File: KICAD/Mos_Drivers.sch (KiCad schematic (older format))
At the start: 15 parts, among them U12 UCC27284-Q1

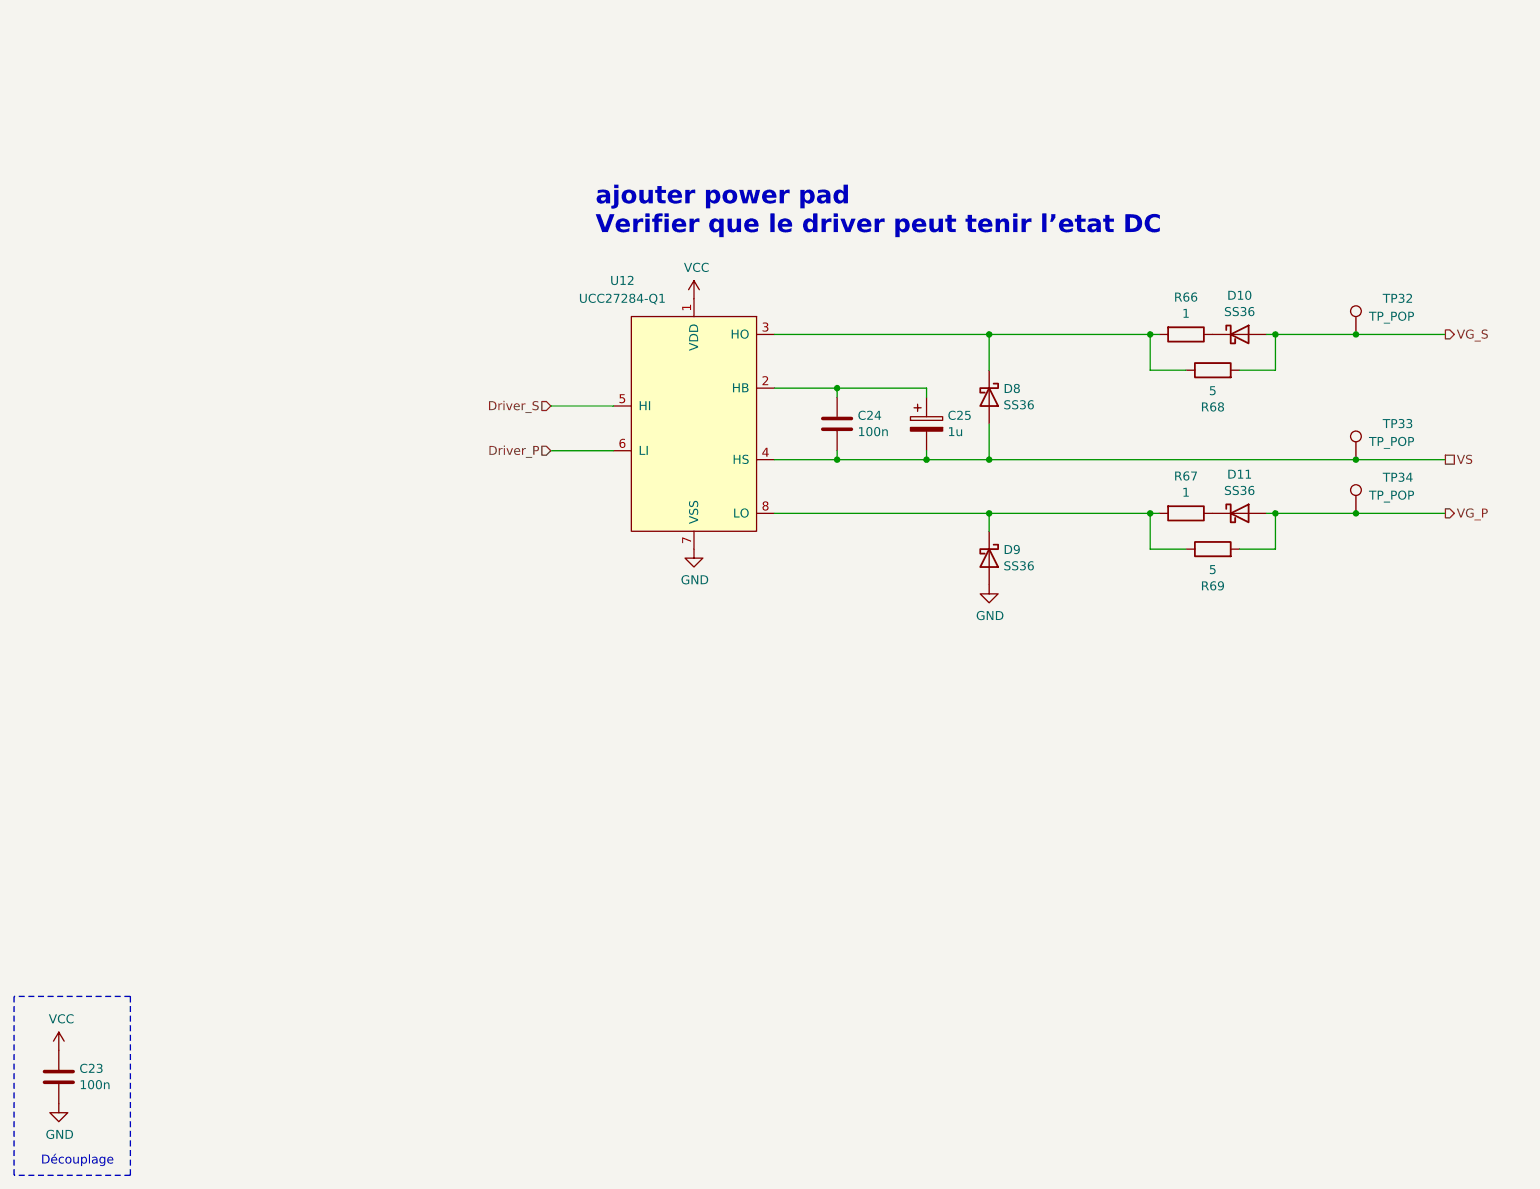
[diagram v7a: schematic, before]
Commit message: added footprint for sepic coil + no more errors in netlist
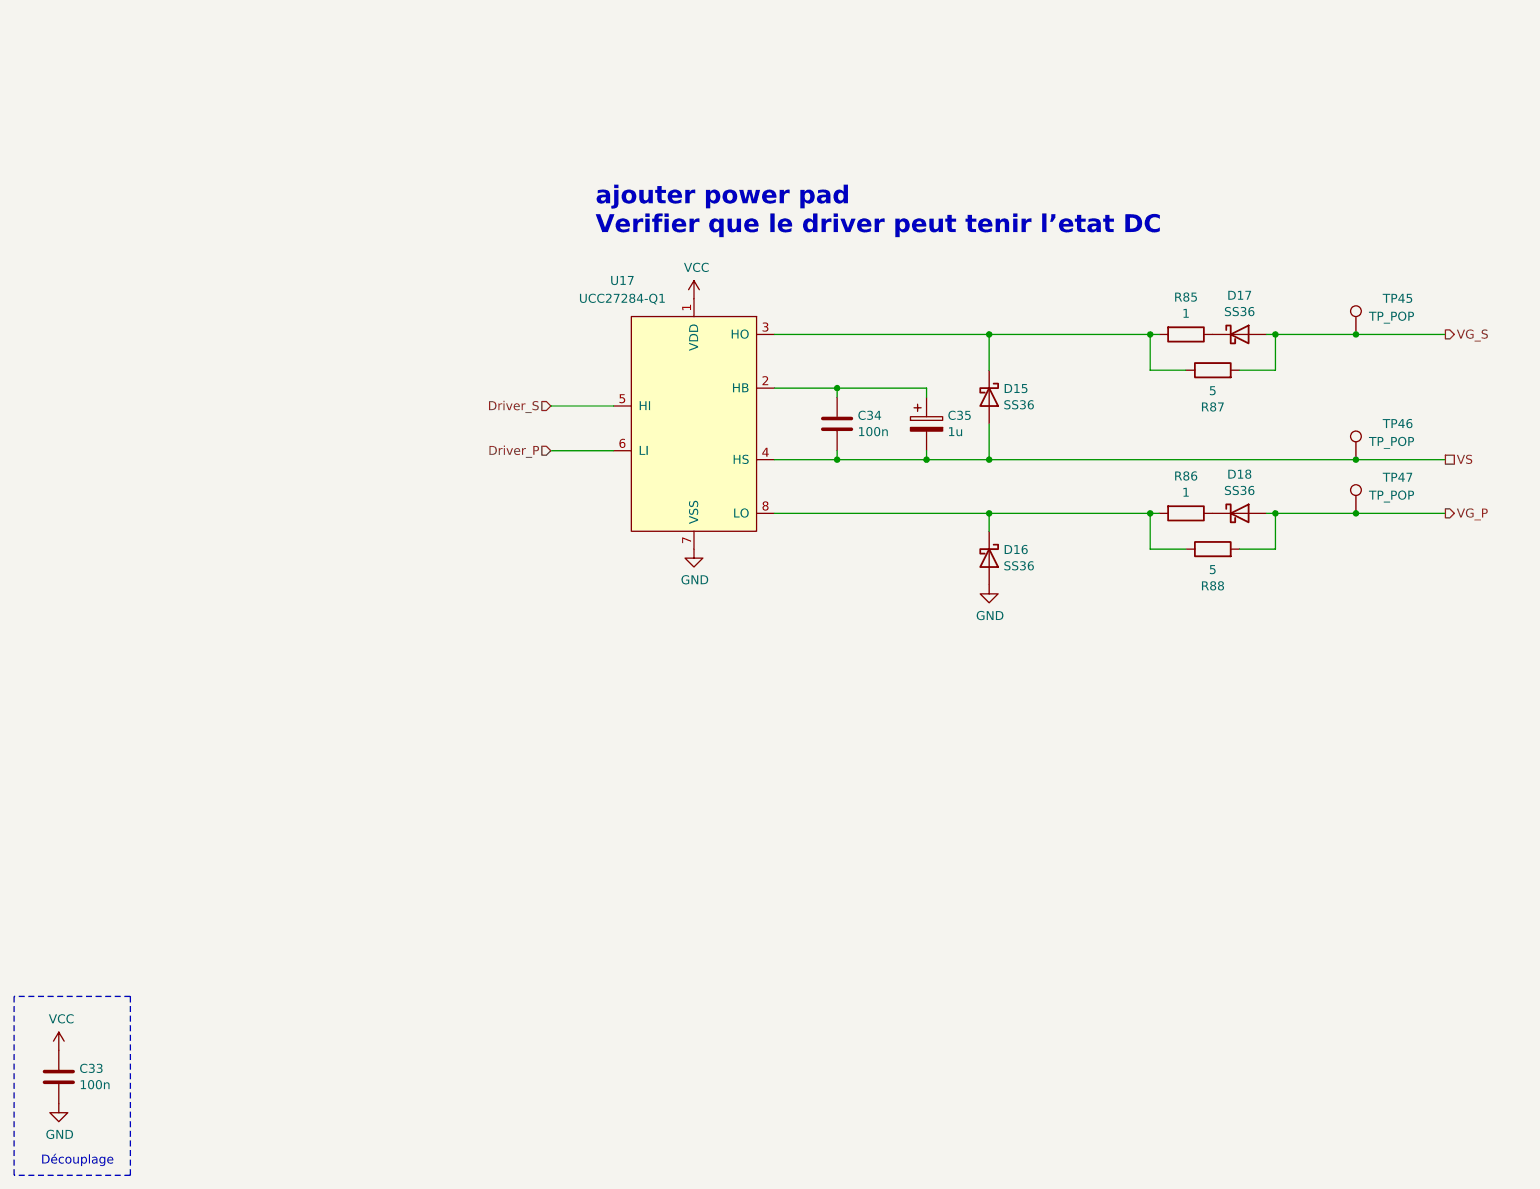
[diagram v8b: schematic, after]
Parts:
- C23, C24, C25: footprint Capacitor_SMD:C_0805_2012Metric_Pad1.15x1.40mm_HandSolder -> Sesame_footprint:C_0805_2012Metric_Pad1.18x1.45mm_HandSolder
- R66, R67, R68, R69: footprint Resistor_SMD:R_0805_2012Metric_Pad1.15x1.40mm_HandSolder -> Sesame_footprint:R_0805_2012Metric_Pad1.20x1.40mm_HandSolder
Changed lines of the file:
@@
 AR Path="/61996C9F/612BC387" Ref="C?"  Part="1"
 AR Path="/619A00BB/612BC387" Ref="C33"  Part="1"
-F 0 "C23" H 965 7146 50  0000 L CNN
+F 0 "C33" H 965 7146 50  0000 L CNN
 F 1 "100n" H 965 7055 50  0000 L CNN
-F 2 "Capacitor_SMD:C_0805_2012Metric_Pad1.15x1.40mm_HandSolder" H 888 6950 50  0001 C CNN
+F 2 "Sesame_footprint:C_0805_2012Metric_Pad1.18x1.45mm_HandSolder" H 888 6950 50  0001 C CNN
 F 3 "~" H 850 7100 50  0001 C CNN
 	1    850  7100
@@
 AR Path="/61996C9F/612C31FB" Ref="D?"  Part="1"
 AR Path="/619A00BB/612C31FB" Ref="D15"  Part="1"
-F 0 "D8" V 6004 3380 50  0000 L CNN
+F 0 "D15" V 6004 3380 50  0000 L CNN
 F 1 "SS36" V 6095 3380 50  0000 L CNN
 F 2 "Diode_SMD:D_SMA_Handsoldering" H 6050 3300 50  0001 C CNN
@@
 AR Path="/61996C9F/6154F3B3" Ref="TP?"  Part="1"
 AR Path="/619A00BB/6154F3B3" Ref="TP46"  Part="1"
-F 0 "TP33" H 8250 3850 50  0000 L CNN
+F 0 "TP46" H 8250 3850 50  0000 L CNN
 F 1 "TP_POP" H 8300 3750 50  0000 C CNN
 F 2 "TestPoint:TestPoint_Loop_D1.80mm_Drill1.0mm_Beaded" H 8300 3650 50  0001 C CNN
@@
 AR Path="/61996C9F/61556ADA" Ref="TP?"  Part="1"
 AR Path="/619A00BB/61556ADA" Ref="TP47"  Part="1"
-F 0 "TP34" H 8250 4150 50  0000 L CNN
+F 0 "TP47" H 8250 4150 50  0000 L CNN
 F 1 "TP_POP" H 8300 4050 50  0000 C CNN
 F 2 "TestPoint:TestPoint_Loop_D1.80mm_Drill1.0mm_Beaded" H 8300 3950 50  0001 C CNN
@@
 AR Path="/61996C9F/61556D55" Ref="TP?"  Part="1"
 AR Path="/619A00BB/61556D55" Ref="TP45"  Part="1"
-F 0 "TP32" H 8250 3150 50  0000 L CNN
+F 0 "TP45" H 8250 3150 50  0000 L CNN
 F 1 "TP_POP" H 8300 3050 50  0000 C CNN
 F 2 "TestPoint:TestPoint_Loop_D1.80mm_Drill1.0mm_Beaded" H 8300 2950 50  0001 C CNN
@@
 AR Path="/61996C9F/615F8500" Ref="U?"  Part="1"
 AR Path="/619A00BB/615F8500" Ref="U17"  Part="1"
-F 0 "U12" H 4000 4250 50  0000 C CNN
+F 0 "U17" H 4000 4250 50  0000 C CNN
 F 1 "UCC27284-Q1" H 4000 4150 50  0000 C CNN
 F 2 "Package_SO:SOIC-8_3.9x4.9mm_P1.27mm" H 4400 3450 50  0001 C CNN
@@
 AR Path="/61996C9F/617A570A" Ref="D?"  Part="1"
 AR Path="/619A00BB/617A570A" Ref="D16"  Part="1"
-F 0 "D9" V 6004 4280 50  0000 L CNN
+F 0 "D16" V 6004 4280 50  0000 L CNN
 F 1 "SS36" V 6095 4280 50  0000 L CNN
 F 2 "Diode_SMD:D_SMA_Handsoldering" H 6050 4200 50  0001 C CNN
@@
 AR Path="/61996C9F/617B4129" Ref="D?"  Part="1"
 AR Path="/619A00BB/617B4129" Ref="D17"  Part="1"
-F 0 "D10" H 7450 3167 50  0000 C CNN
+F 0 "D17" H 7450 3167 50  0000 C CNN
 F 1 "SS36" H 7450 3076 50  0000 C CNN
 F 2 "Diode_SMD:D_SMA_Handsoldering" H 7450 2950 50  0001 C CNN
@@
 AR Path="/61996C9F/617C4D4F" Ref="R?"  Part="1"
 AR Path="/619A00BB/617C4D4F" Ref="R85"  Part="1"
-F 0 "R66" V 6943 2950 50  0000 C CNN
+F 0 "R85" V 6943 2950 50  0000 C CNN
 F 1 "1" V 7034 2950 50  0000 C CNN
-F 2 "Resistor_SMD:R_0805_2012Metric_Pad1.15x1.40mm_HandSolder" V 7080 2950 50  0001 C CNN
+F 2 "Sesame_footprint:R_0805_2012Metric_Pad1.20x1.40mm_HandSolder" V 7080 2950 50  0001 C CNN
 F 3 "~" H 7150 2950 50  0001 C CNN
 	1    7150 2950
@@
 AR Path="/61996C9F/617CA6D6" Ref="R?"  Part="1"
 AR Path="/619A00BB/617CA6D6" Ref="R87"  Part="1"
-F 0 "R68" V 7093 3150 50  0000 C CNN
+F 0 "R87" V 7093 3150 50  0000 C CNN
 F 1 "5" V 7184 3150 50  0000 C CNN
-F 2 "Resistor_SMD:R_0805_2012Metric_Pad1.15x1.40mm_HandSolder" V 7230 3150 50  0001 C CNN
+F 2 "Sesame_footprint:R_0805_2012Metric_Pad1.20x1.40mm_HandSolder" V 7230 3150 50  0001 C CNN
 F 3 "~" H 7300 3150 50  0001 C CNN
 	1    7300 3150
@@
 AR Path="/60F19D6C/619F44C6" Ref="C25"  Part="1"
 AR Path="/619A00BB/619F44C6" Ref="C35"  Part="1"
-F 0 "C25" H 5818 3496 50  0000 L CNN
+F 0 "C35" H 5818 3496 50  0000 L CNN
 F 1 "1u" H 5818 3405 50  0000 L CNN
-F 2 "Capacitor_SMD:C_0805_2012Metric_Pad1.15x1.40mm_HandSolder" H 5738 3300 50  0001 C CNN
+F 2 "Sesame_footprint:C_0805_2012Metric_Pad1.18x1.45mm_HandSolder" H 5738 3300 50  0001 C CNN
 F 3 "~" H 5700 3450 50  0001 C CNN
 	1    5700 3450
@@
 AR Path="/61996C9F/61A058A4" Ref="D?"  Part="1"
 AR Path="/619A00BB/61A058A4" Ref="D18"  Part="1"
-F 0 "D11" H 7450 4167 50  0000 C CNN
+F 0 "D18" H 7450 4167 50  0000 C CNN
 F 1 "SS36" H 7450 4076 50  0000 C CNN
 F 2 "Diode_SMD:D_SMA_Handsoldering" H 7450 3950 50  0001 C CNN
@@
 AR Path="/61996C9F/61A058AA" Ref="R?"  Part="1"
 AR Path="/619A00BB/61A058AA" Ref="R86"  Part="1"
-F 0 "R67" V 6943 3950 50  0000 C CNN
+F 0 "R86" V 6943 3950 50  0000 C CNN
 F 1 "1" V 7034 3950 50  0000 C CNN
-F 2 "Resistor_SMD:R_0805_2012Metric_Pad1.15x1.40mm_HandSolder" V 7080 3950 50  0001 C CNN
+F 2 "Sesame_footprint:R_0805_2012Metric_Pad1.20x1.40mm_HandSolder" V 7080 3950 50  0001 C CNN
 F 3 "~" H 7150 3950 50  0001 C CNN
 	1    7150 3950
@@
 AR Path="/61996C9F/61A058B0" Ref="R?"  Part="1"
 AR Path="/619A00BB/61A058B0" Ref="R88"  Part="1"
-F 0 "R69" V 7093 4150 50  0000 C CNN
+F 0 "R88" V 7093 4150 50  0000 C CNN
 F 1 "5" V 7184 4150 50  0000 C CNN
-F 2 "Resistor_SMD:R_0805_2012Metric_Pad1.15x1.40mm_HandSolder" V 7230 4150 50  0001 C CNN
+F 2 "Sesame_footprint:R_0805_2012Metric_Pad1.20x1.40mm_HandSolder" V 7230 4150 50  0001 C CNN
 F 3 "~" H 7300 4150 50  0001 C CNN
 	1    7300 4150
@@
 AR Path="/61996C9F/61A06D05" Ref="C?"  Part="1"
 AR Path="/619A00BB/61A06D05" Ref="C34"  Part="1"
-F 0 "C24" H 5315 3496 50  0000 L CNN
+F 0 "C34" H 5315 3496 50  0000 L CNN
 F 1 "100n" H 5315 3405 50  0000 L CNN
-F 2 "Capacitor_SMD:C_0805_2012Metric_Pad1.15x1.40mm_HandSolder" H 5238 3300 50  0001 C CNN
+F 2 "Sesame_footprint:C_0805_2012Metric_Pad1.18x1.45mm_HandSolder" H 5238 3300 50  0001 C CNN
 F 3 "~" H 5200 3450 50  0001 C CNN
 	1    5200 3450
